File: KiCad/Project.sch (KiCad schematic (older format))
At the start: 6 parts, among them IC1 ATMEGA328-P, U1 BlueSmirf

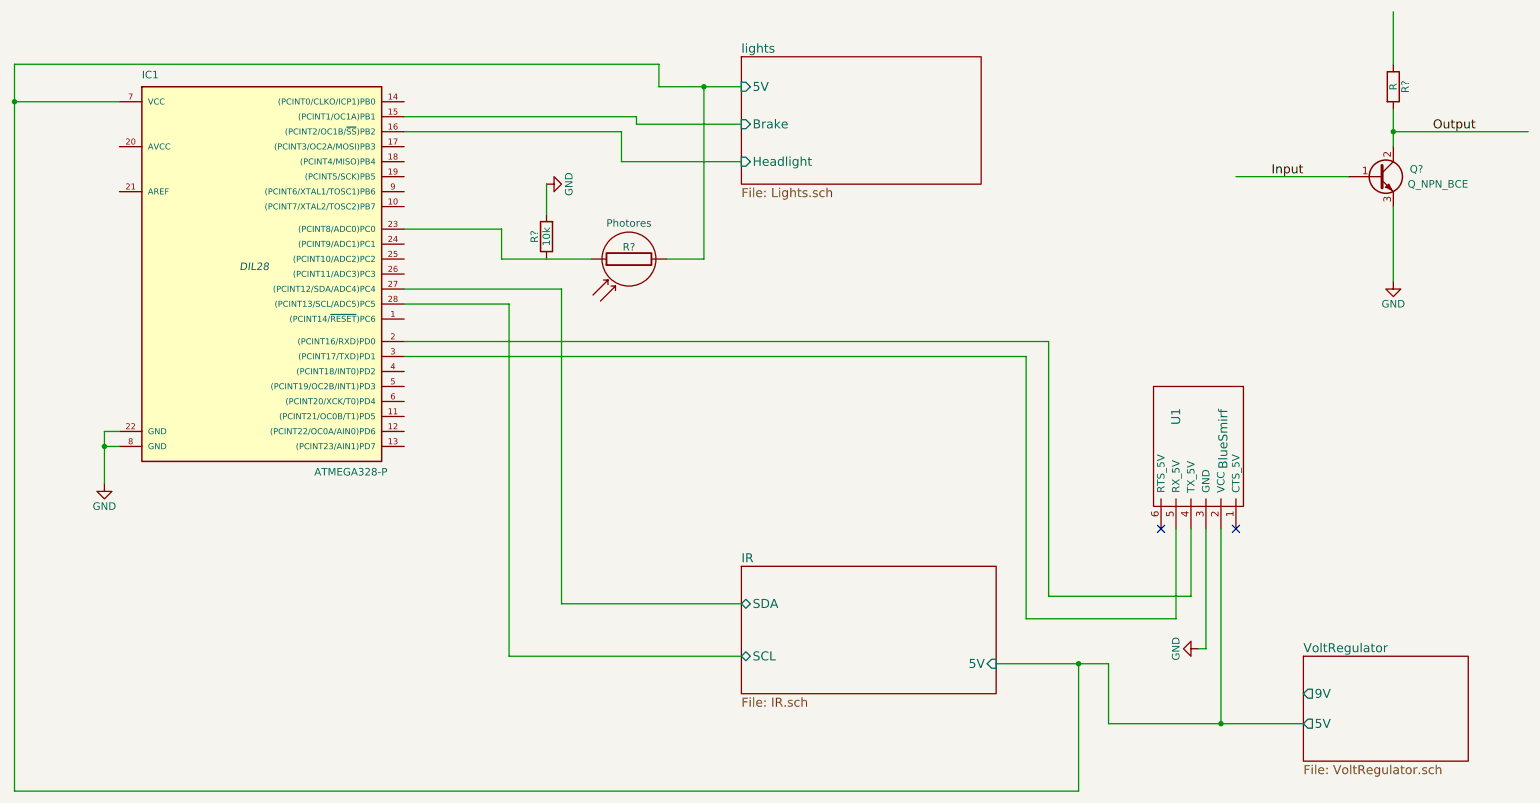
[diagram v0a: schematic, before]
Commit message: Added the Hbridge
The schematics is almost completed with all the values set on resitors
and all the components should be there. Minor changes is to be expected
though.
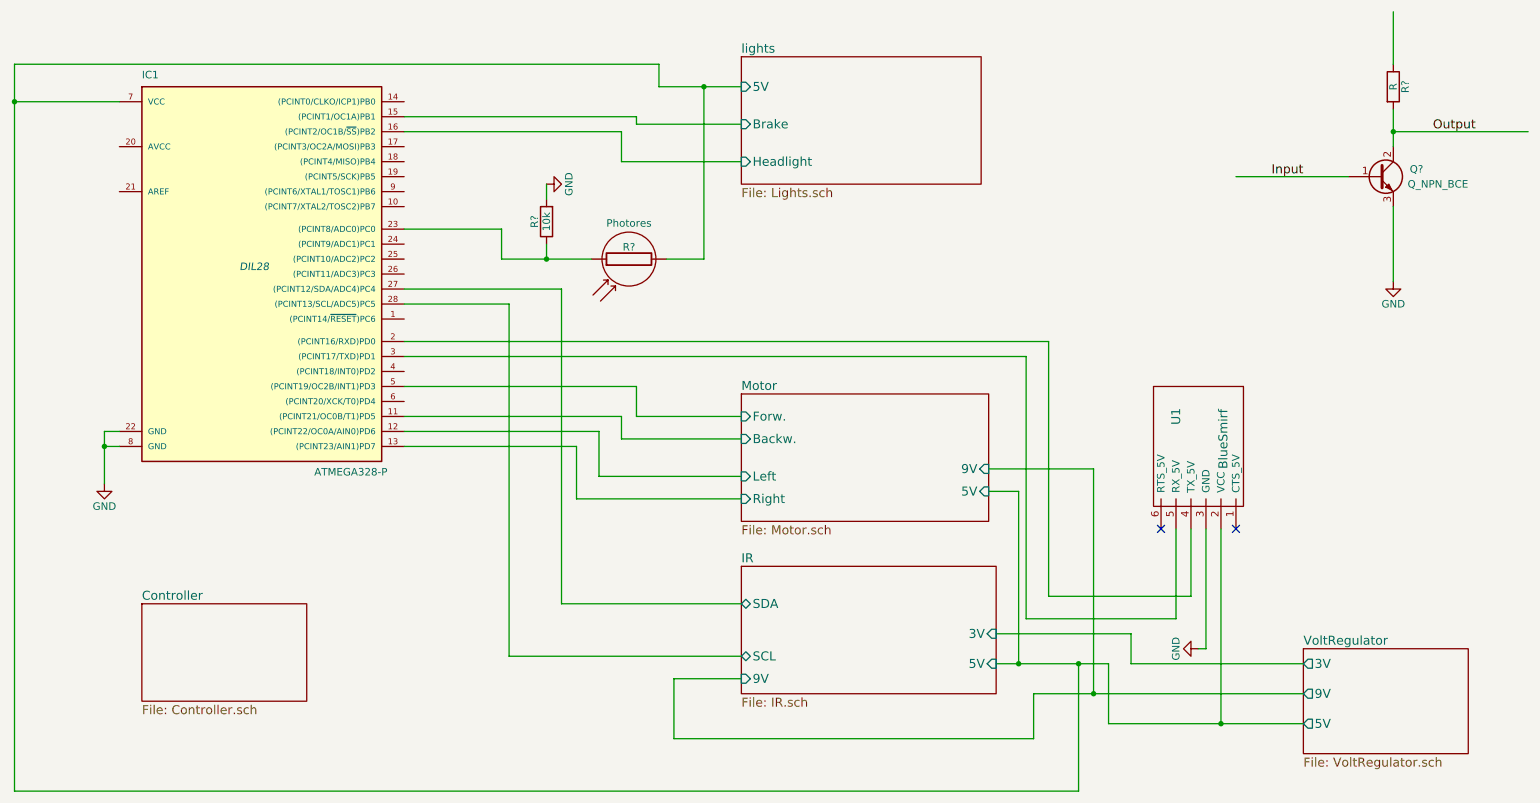
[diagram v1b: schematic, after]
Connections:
- wire segments 47 -> 72
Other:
- moved on the sheet: R?
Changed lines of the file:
@@
 LIBS:valves
 LIBS:ir_recieve
+LIBS:I2C_LCD
+LIBS:LinkuraModule
+LIBS:i2cdisplay
+LIBS:ca3240e
+LIBS:SN754410NE
+LIBS:motor
 LIBS:Project-cache
 EELAYER 25 0
@@
 $Descr A4 11693 8268
 encoding utf-8
-Sheet 1 4
+Sheet 1 7
 Title ""
 Date ""
@@
 Connection ~ 1500 3550
 $Sheet
-S 9500 4950 1100 700
+S 9500 4900 1100 700
 U 57160B94
 F0 "VoltRegulator" 60
@@
 F2 "9V" O L 9500 5200 60
 F3 "5V" O L 9500 5400 60
+F4 "3V" O L 9500 5000 60
 $EndSheet
 $Comp
@@
 F3 "SDA" B L 5750 4600 60
 F4 "SCL" B L 5750 4950 60
-$EndSheet
-Wire Wire Line
-	9500 5400 8200 5400
+F5 "9V" I L 5750 5100 60
+F6 "3V" I R 7450 4800 60
+$EndSheet
 Wire Wire Line
 	8200 5400 8200 5000
@@
 L R R?
 U 1 1 5716E4CF
-P 4450 2150
-F 0 "R?" V 4530 2150 50  0000 C CNN
-F 1 "10k" V 4450 2150 50  0000 C CNN
-F 2 "" V 4380 2150 50  0000 C CNN
-F 3 "" H 4450 2150 50  0000 C CNN
-	1    4450 2150
+P 4450 2050
+F 0 "R?" V 4530 2050 50  0000 C CNN
+F 1 "10k" V 4450 2050 50  0000 C CNN
+F 2 "" V 4380 2050 50  0000 C CNN
+F 3 "" H 4450 2050 50  0000 C CNN
+	1    4450 2050
 	-1   0    0    1
 $EndComp
@@
 $EndComp
 Wire Wire Line
-	4450 2000 4450 1800
-Wire Wire Line
 	3500 2500 4550 2500
 Wire Wire Line
@@
 Wire Wire Line
 	4200 2600 3500 2600
+$Sheet
+S 1750 4600 1100 650
+U 5717B094
+F0 "Controller" 60
+F1 "Controller.sch" 60
+$EndSheet
+Wire Wire Line
+	8200 5400 9500 5400
+Wire Wire Line
+	9500 5000 8350 5000
+Wire Wire Line
+	8350 5000 8350 4800
+Wire Wire Line
+	8350 4800 7450 4800
+Wire Wire Line
+	9500 5200 7700 5200
+Wire Wire Line
+	7700 5200 7700 5500
+Wire Wire Line
+	7700 5500 5300 5500
+Wire Wire Line
+	5300 5500 5300 5100
+Wire Wire Line
+	5300 5100 5750 5100
+Wire Wire Line
+	4450 1800 4450 1900
+Wire Wire Line
+	4450 2200 4450 2300
+Connection ~ 4450 2300
+$Sheet
+S 5750 3200 1650 850
+U 571BEA93
+F0 "Motor" 60
+F1 "Motor.sch" 60
+F2 "Forw." I L 5750 3350 60
+F3 "Backw." I L 5750 3500 60
+F4 "5V" I R 7400 3850 60
+F5 "9V" I R 7400 3700 60
+F6 "Right" I L 5750 3900 60
+F7 "Left" I L 5750 3750 60
+$EndSheet
+Wire Wire Line
+	5750 3350 5050 3350
+Wire Wire Line
+	5050 3350 5050 3150
+Wire Wire Line
+	5050 3150 3500 3150
+Wire Wire Line
+	5750 3500 4950 3500
+Wire Wire Line
+	4950 3500 4950 3350
+Wire Wire Line
+	4950 3350 3500 3350
+Wire Wire Line
+	5750 3750 4800 3750
+Wire Wire Line
+	4800 3750 4800 3450
+Wire Wire Line
+	4800 3450 3500 3450
+Wire Wire Line
+	5750 3900 4650 3900
+Wire Wire Line
+	4650 3900 4650 3550
+Wire Wire Line
+	4650 3550 3500 3550
+Wire Wire Line
+	7600 5000 7600 3850
+Wire Wire Line
+	7600 3850 7400 3850
+Connection ~ 7600 5000
+Wire Wire Line
+	8100 5200 8100 3700
+Wire Wire Line
+	8100 3700 7400 3700
+Connection ~ 8100 5200
 $EndSCHEMATC

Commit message: Updated the schematics and started with the PCB
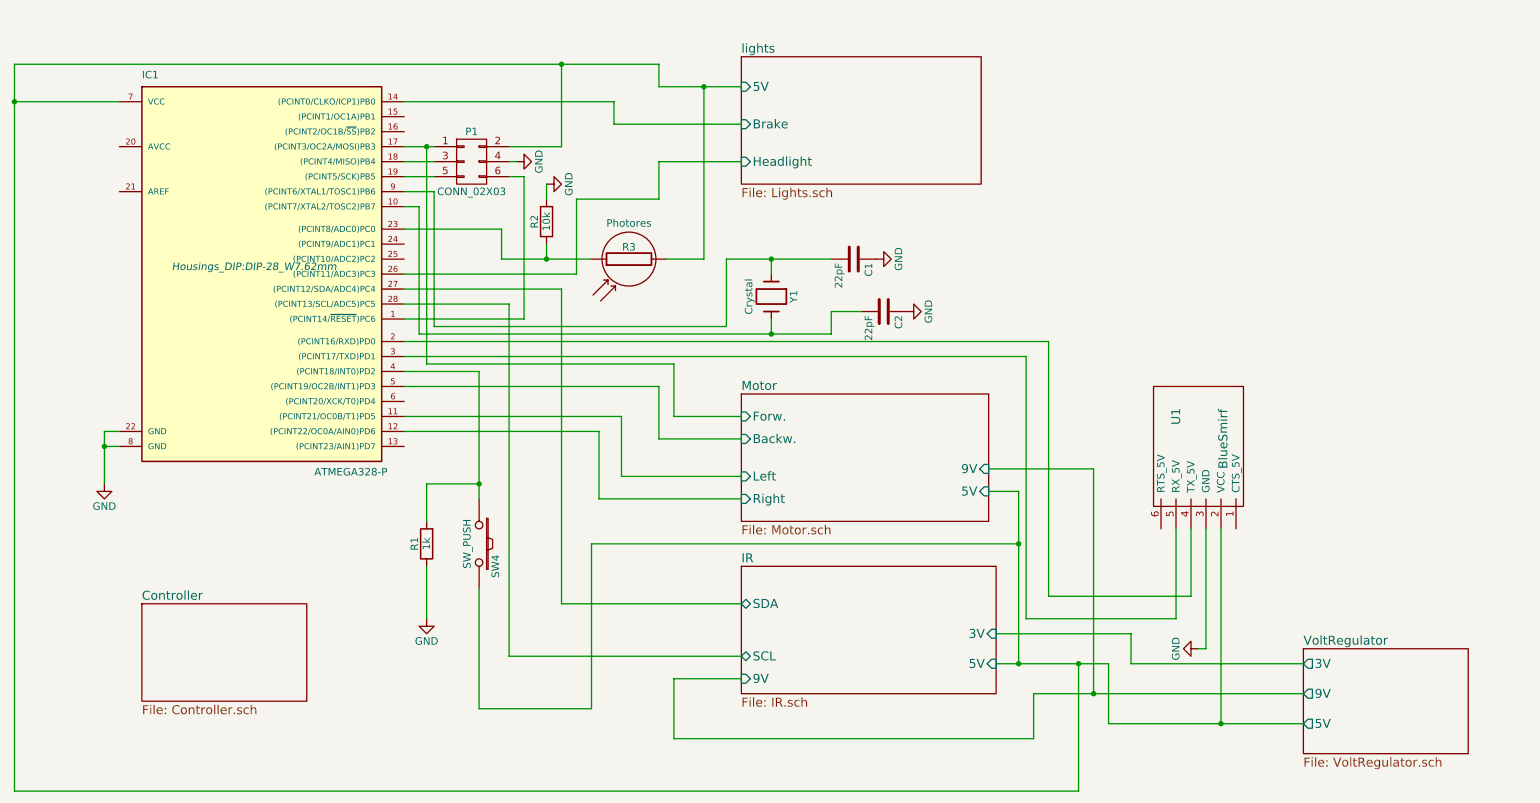
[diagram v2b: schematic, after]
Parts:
- removed Q?: Q_NPN_BCE, symbol Q_NPN_BCE
- removed R?: R, symbol R
- added C1, C2: 22pF, Capacitors_ThroughHole:C_Disc_D3_P2.5, symbol C
- added P1: CONN_02X03, Pin_Headers:Pin_Header_Angled_2x03, symbol CONN_02X03
- added R1: 1k, Resistors_ThroughHole:Resistor_Vertical_RM5mm, symbol R
- added SW4: SW_PUSH, Wire_Connections_Bridges:WireConnection_1.50mmDrill, symbol SW_PUSH
- added Y1: Crystal, Crystals:Crystal_HC52-U_Vertical, symbol Crystal
- IC1: footprint DIL28 -> Housings_DIP:DIP-28_W7.62mm
- R2: renamed from R?; footprint (none) -> Resistors_ThroughHole:Resistor_Vertical_RM5mm
- R3: renamed from R?; footprint (none) -> Wire_Connections_Bridges:WireConnection_1.50mmDrill
- U1: footprint (none) -> Pin_Headers:Pin_Header_Straight_1x06
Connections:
- net labels removed: Input, Output
- wire segments 72 -> 100
- no-connect marks 2 -> 0

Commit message: Started with the PCB
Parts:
- added P2: CONN_01X02, Pin_Headers:Pin_Header_Straight_1x02, symbol CONN_01X02
- P1: footprint Pin_Headers:Pin_Header_Angled_2x03 -> Pin_Headers:Pin_Header_Straight_2x03
- U1: footprint Pin_Headers:Pin_Header_Straight_1x06 -> Pin_Headers:Pin_Header_Straight_1x06_Pitch2.00mm
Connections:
- net IR/5V: no longer P1.2 (P2)
- net at IC1.2 ((PCINT16/RXD)PD0), U1.4 (TX_5V): now also P2.1 (P1)
- net at IC1.3 ((PCINT17/TXD)PD1), U1.5 (RX_5V): now also P2.2 (P2)
- no-connect marks 0 -> 10
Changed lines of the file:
@@
 $Descr A4 11693 8268
 encoding utf-8
-Sheet 1 6
+Sheet 1 5
 Title ""
 Date ""
@@
 F 0 "U1" H 8600 3400 60  0000 C CNN
 F 1 "BlueSmirf" H 8750 3750 60  0000 C TNN
-F 2 "Pin_Headers:Pin_Header_Straight_1x06" H 8800 3550 60  0001 C CNN
+F 2 "Pin_Headers:Pin_Header_Straight_1x06_Pitch2.00mm" H 8800 3550 60  0001 C CNN
 F 3 "" H 8800 3550 60  0000 C CNN
 	1    8800 3550
@@
 Wire Wire Line
 	4200 2600 3500 2600
-$Sheet
-S 1750 4600 1100 650
-U 5717B094
-F0 "Controller" 60
-F1 "Controller.sch" 60
-$EndSheet
 Wire Wire Line
 	8200 5400 9500 5400
@@
 F 0 "P1" H 3950 1850 50  0000 C CNN
 F 1 "CONN_02X03" H 3950 1450 50  0000 C CNN
-F 2 "Pin_Headers:Pin_Header_Angled_2x03" H 3950 450 50  0001 C CNN
+F 2 "Pin_Headers:Pin_Header_Straight_2x03" H 3950 450 50  0001 C CNN
 F 3 "" H 3950 450 50  0000 C CNN
 	1    3950 1650
@@
 Wire Wire Line
 	3700 1750 3500 1750
-Wire Wire Line
-	4550 1000 4550 1550
-Wire Wire Line
-	4550 1550 4200 1550
-Connection ~ 4550 1000
 Wire Wire Line
 	4200 1750 4300 1750
@@
 Wire Wire Line
 	5200 3500 5750 3500
+$Comp
+L CONN_01X02 P2
+U 1 1 5734FE54
+P 8350 2400
+F 0 "P2" H 8350 2550 50  0000 C CNN
+F 1 "CONN_01X02" V 8450 2400 50  0000 C CNN
+F 2 "Pin_Headers:Pin_Header_Straight_1x02" H 8350 2400 50  0001 C CNN
+F 3 "" H 8350 2400 50  0000 C CNN
+	1    8350 2400
+	1    0    0    -1
+$EndComp
+Wire Wire Line
+	8150 2350 7450 2350
+Wire Wire Line
+	7450 2350 7450 2850
+Connection ~ 7450 2850
+Wire Wire Line
+	7550 2450 7550 2950
+Wire Wire Line
+	7550 2450 8150 2450
+Connection ~ 7550 2950
+NoConn ~ 4200 1550
+NoConn ~ 8550 4100
+NoConn ~ 9050 4100
+NoConn ~ 3500 1350
+NoConn ~ 3500 1450
+NoConn ~ 3500 2200
+NoConn ~ 3500 2300
+NoConn ~ 3500 3250
+NoConn ~ 3500 3550
+NoConn ~ 1600 1550
 $EndSCHEMATC

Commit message: Added smaller footprints
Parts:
- R3, SW4: footprint Wire_Connections_Bridges:WireConnection_1.50mmDrill -> Wire_Pads:SolderWirePad_2x_1mmDrill
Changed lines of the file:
@@
 $EndComp
 $Comp
-L GND #PWR1
+L GND #PWR01
 U 1 1 5715DC43
 P 1500 3800
-F 0 "#PWR1" H 1500 3550 50  0001 C CNN
+F 0 "#PWR01" H 1500 3550 50  0001 C CNN
 F 1 "GND" H 1500 3650 50  0000 C CNN
 F 2 "" H 1500 3800 50  0000 C CNN
@@
 	8850 4900 8800 4900
 $Comp
-L GND #PWR7
+L GND #PWR02
 U 1 1 57165880
 P 8800 4900
-F 0 "#PWR7" H 8800 4650 50  0001 C CNN
+F 0 "#PWR02" H 8800 4650 50  0001 C CNN
 F 1 "GND" H 8800 4750 50  0000 C CNN
 F 2 "" H 8800 4900 50  0000 C CNN
@@
 F 0 "R3" V 5080 2300 50  0000 C CNN
 F 1 "Photores" V 5210 2300 50  0000 C TNN
-F 2 "Wire_Connections_Bridges:WireConnection_1.50mmDrill" V 4930 2300 50  0001 C CNN
+F 2 "Wire_Pads:SolderWirePad_2x_1mmDrill" V 4930 2300 50  0001 C CNN
 F 3 "" H 5000 2300 50  0000 C CNN
 	1    5000 2300
@@
 	4150 2100 3500 2100
 $Comp
-L GND #PWR4
+L GND #PWR03
 U 1 1 5716EE89
 P 4450 1800
-F 0 "#PWR4" H 4450 1550 50  0001 C CNN
+F 0 "#PWR03" H 4450 1550 50  0001 C CNN
 F 1 "GND" H 4450 1650 50  0000 C CNN
 F 2 "" H 4450 1800 50  0000 C CNN
@@
 	4300 2700 3500 2700
 $Comp
-L GND #PWR3
+L GND #PWR04
 U 1 1 5733AA01
 P 4250 1650
-F 0 "#PWR3" H 4250 1400 50  0001 C CNN
+F 0 "#PWR04" H 4250 1400 50  0001 C CNN
 F 1 "GND" H 4250 1500 50  0000 C CNN
 F 2 "" H 4250 1650 50  0000 C CNN
@@
 $EndComp
 $Comp
-L GND #PWR5
+L GND #PWR05
 U 1 1 5733D1EA
 P 6650 2300
-F 0 "#PWR5" H 6650 2050 50  0001 C CNN
+F 0 "#PWR05" H 6650 2050 50  0001 C CNN
 F 1 "GND" H 6650 2150 50  0000 C CNN
 F 2 "" H 6650 2300 50  0000 C CNN
@@
 $EndComp
 $Comp
-L GND #PWR6
+L GND #PWR06
 U 1 1 5733D278
 P 6850 2650
-F 0 "#PWR6" H 6850 2400 50  0001 C CNN
+F 0 "#PWR06" H 6850 2400 50  0001 C CNN
 F 1 "GND" H 6850 2500 50  0000 C CNN
 F 2 "" H 6850 2650 50  0000 C CNN
@@
 F 0 "SW4" H 4150 4310 50  0000 C CNN
 F 1 "SW_PUSH" H 4000 4120 50  0000 C CNN
-F 2 "Wire_Connections_Bridges:WireConnection_1.50mmDrill" H 4000 4200 50  0001 C CNN
+F 2 "Wire_Pads:SolderWirePad_2x_1mmDrill" H 4000 4200 50  0001 C CNN
 F 3 "" H 4000 4200 50  0000 C CNN
 	1    4000 4200
@@
 $EndComp
 $Comp
-L GND #PWR2
+L GND #PWR07
 U 1 1 5734269F
 P 3650 4700
-F 0 "#PWR2" H 3650 4450 50  0001 C CNN
+F 0 "#PWR07" H 3650 4450 50  0001 C CNN
 F 1 "GND" H 3650 4550 50  0000 C CNN
 F 2 "" H 3650 4700 50  0000 C CNN
